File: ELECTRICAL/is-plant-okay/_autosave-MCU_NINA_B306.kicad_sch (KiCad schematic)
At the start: 1 part

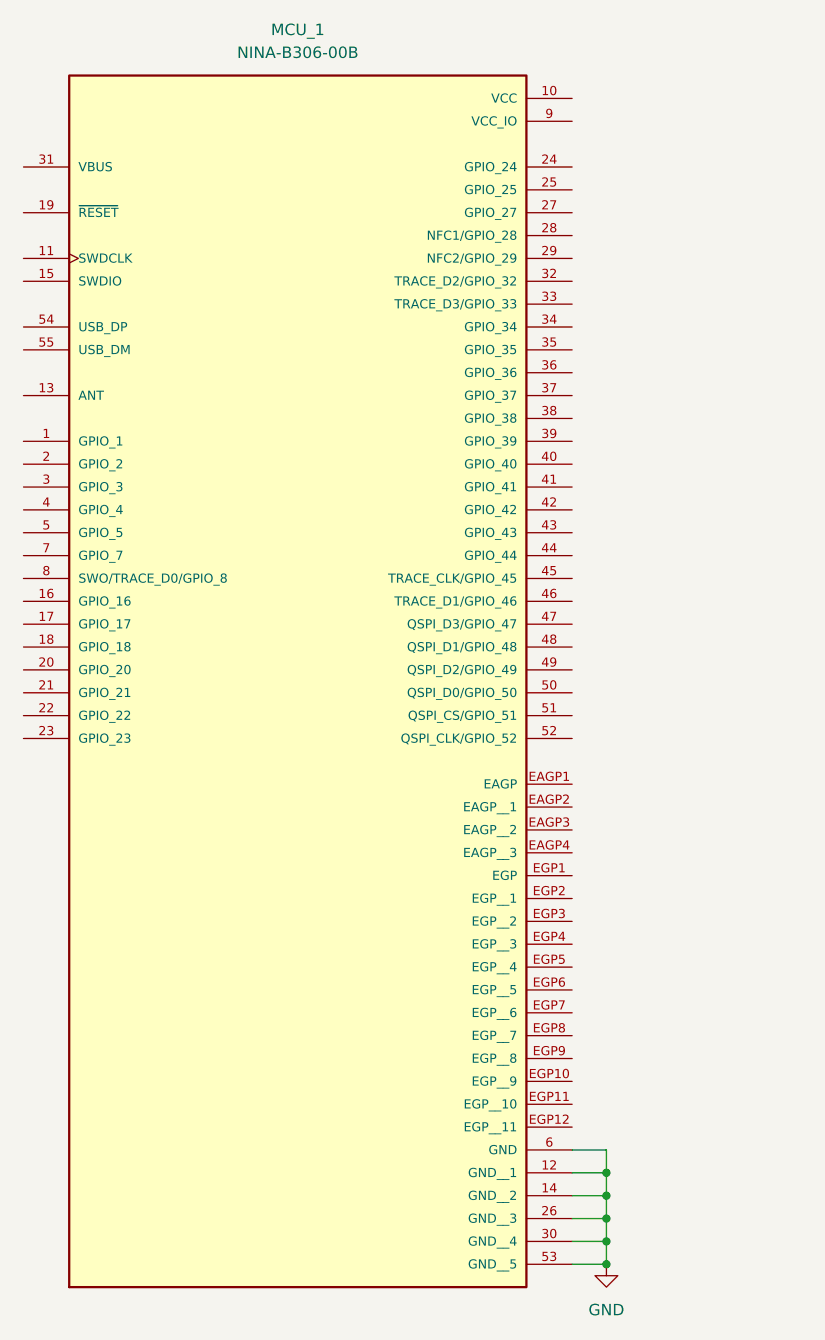
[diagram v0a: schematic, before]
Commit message: feat: add ldo and power management IC
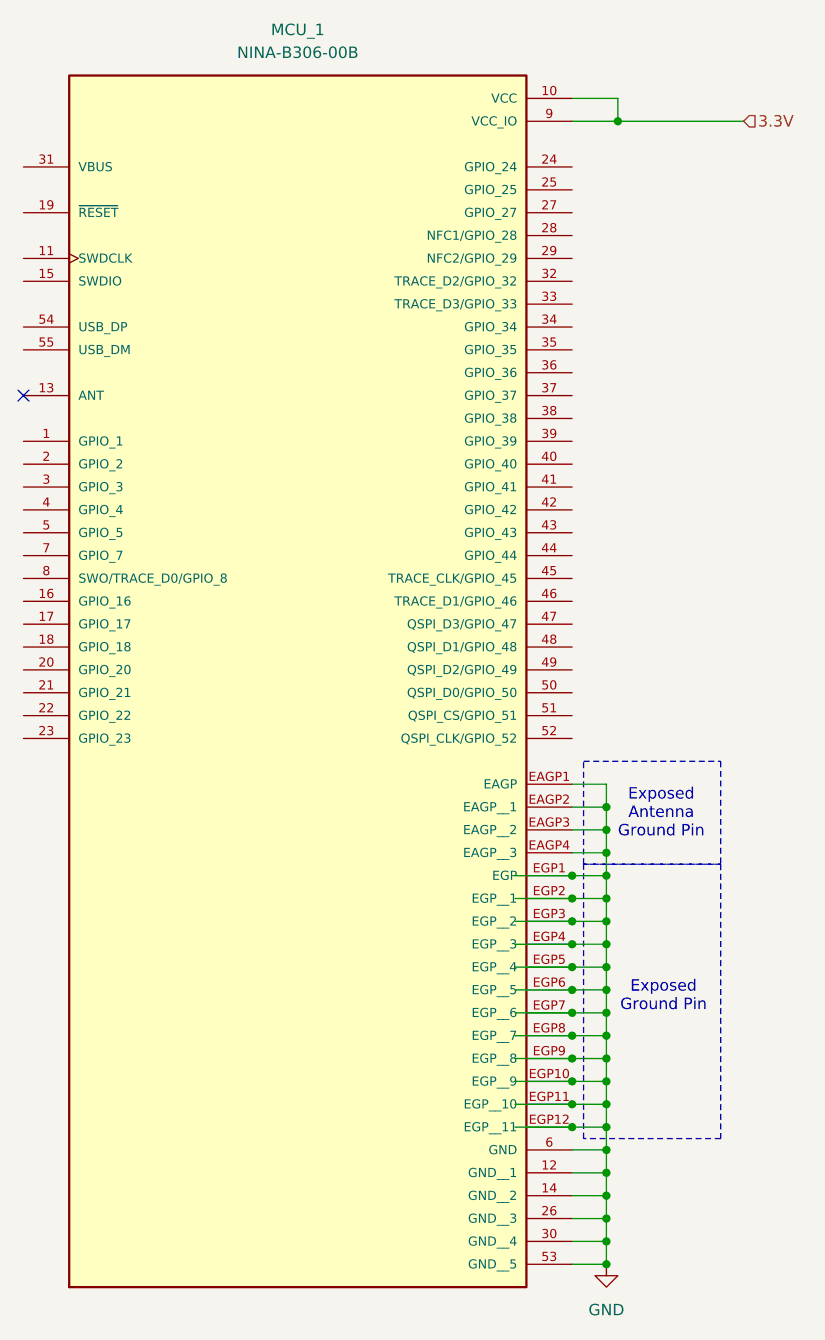
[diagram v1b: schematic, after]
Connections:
- net GND: now also MCU_1.EAGP1 (EAGP), MCU_1.EAGP2 (EAGP__1), MCU_1.EAGP3 (EAGP__2), MCU_1.EAGP4 (EAGP__3), MCU_1.EGP1 (EGP), MCU_1.EGP10 (EGP__9), MCU_1.EGP11 (EGP__10), MCU_1.EGP12 (EGP__11), MCU_1.EGP2 (EGP__1), MCU_1.EGP3 (EGP__2), MCU_1.EGP4 (EGP__3), MCU_1.EGP5 (EGP__4), MCU_1.EGP6 (EGP__5), MCU_1.EGP7 (EGP__6), MCU_1.EGP8 (EGP__7), MCU_1.EGP9 (EGP__8)
- net 3.3V: now reaches MCU_1.10 (VCC)
- net 3.3V: now also MCU_1.9 (VCC_IO)
- no-connect marks 0 -> 1
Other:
- note added: "Exposed Antenna Ground Pin"
- note added: "Exposed Ground Pin"
